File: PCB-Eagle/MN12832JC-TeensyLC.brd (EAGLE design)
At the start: 206.7 x 45.7 mm, 46 parts, among them IC4 ZXBM5210, IC6 74HC132D, SW3 EC12E_SW, SW4 EC12E_SW

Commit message: fixed Up Converter R9/R10 twist, adjusted values for 50V
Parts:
- R10: value 1k -> 39
- R9: value 39 -> 1.5k
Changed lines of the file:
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@@
 <?xml version="1.0" encoding="utf-8"?>
 <!DOCTYPE eagle SYSTEM "eagle.dtd">
-<eagle version="9.5.2">
+<eagle version="9.5.1">
 <drawing>
 <settings>
@@
 <layers>
 <layer number="1" name="Top" color="4" fill="1" visible="yes" active="yes"/>
-<layer number="16" name="Bottom" color="1" fill="1" visible="yes" active="yes"/>
+<layer number="16" name="Bottom" color="1" fill="1" visible="no" active="yes"/>
 <layer number="17" name="Pads" color="2" fill="1" visible="yes" active="yes"/>
 <layer number="18" name="Vias" color="2" fill="1" visible="yes" active="yes"/>
@@
 <layer number="20" name="Dimension" color="24" fill="1" visible="yes" active="yes"/>
 <layer number="21" name="tPlace" color="7" fill="1" visible="yes" active="yes"/>
-<layer number="22" name="bPlace" color="7" fill="1" visible="yes" active="yes"/>
+<layer number="22" name="bPlace" color="7" fill="1" visible="no" active="yes"/>
 <layer number="23" name="tOrigins" color="15" fill="1" visible="yes" active="yes"/>
 <layer number="24" name="bOrigins" color="15" fill="1" visible="yes" active="yes"/>
@@
 <attribute name="NAME" x="123.19" y="19.05" size="1.27" layer="25" rot="R270"/>
 <attribute name="SPICEPREFIX" value="C" x="121.92" y="17.78" size="1.778" layer="27" rot="R270" display="off"/>
-<attribute name="VALUE" x="119.38" y="19.05" size="1.27" layer="27" rot="R270"/>
+<attribute name="VALUE" x="120.142" y="13.716" size="1.27" layer="27"/>
 </element>
 <element name="R8" library="rcl" library_urn="urn:adsk.eagle:library:334" package="R1206" package3d_urn="urn:adsk.eagle:package:23540/2" value="2.7k" x="125.73" y="17.78" smashed="yes" rot="R270">
 <attribute name="NAME" x="127" y="19.05" size="1.27" layer="25" rot="R270"/>
 <attribute name="SPICEPREFIX" value="R" x="125.73" y="17.78" size="1.778" layer="27" rot="R270" display="off"/>
-<attribute name="VALUE" x="123.19" y="19.05" size="1.27" layer="27" rot="R270"/>
+<attribute name="VALUE" x="124.333" y="13.716" size="1.27" layer="27"/>
 </element>
 <element name="IC4" library="vfds" package="SO8" value="ZXBM5210" x="134.62" y="35.56" smashed="yes" rot="R180">
 <attribute name="NAME" x="137.795" y="37.465" size="1.27" layer="25" rot="R270"/>
 <attribute name="PARTNAME" value="ZXBM5210" x="134.62" y="35.56" size="1.778" layer="27" rot="R180" display="off"/>
-<attribute name="VALUE" x="130.175" y="37.465" size="1.27" layer="27" rot="R270"/>
+<attribute name="VALUE" x="130.429" y="38.989" size="1.27" layer="27"/>
 </element>
 <element name="IC5" library="vfds" package="TO263-5" package3d_urn="urn:adsk.eagle:package:16438/2" value="" x="92.71" y="30.48" smashed="yes">
@@
 <attribute name="VALUE" x="106.299" y="33.401" size="1.27" layer="27" rot="R90"/>
 </element>
-<element name="R9" library="rcl" library_urn="urn:adsk.eagle:library:334" package="R1206" package3d_urn="urn:adsk.eagle:package:23540/2" value="39" x="95.25" y="19.05" smashed="yes">
+<element name="R9" library="rcl" library_urn="urn:adsk.eagle:library:334" package="R1206" package3d_urn="urn:adsk.eagle:package:23540/2" value="1.5k" x="95.25" y="19.05" smashed="yes">
 <attribute name="NAME" x="93.98" y="20.32" size="1.27" layer="25"/>
 <attribute name="SPICEPREFIX" value="R" x="95.25" y="19.05" size="1.778" layer="27" display="off"/>
 <attribute name="VALUE" x="93.98" y="16.51" size="1.27" layer="27"/>
 </element>
-<element name="R10" library="rcl" library_urn="urn:adsk.eagle:library:334" package="R1206" package3d_urn="urn:adsk.eagle:package:23540/2" value="1k" x="88.9" y="19.05" smashed="yes">
+<element name="R10" library="rcl" library_urn="urn:adsk.eagle:library:334" package="R1206" package3d_urn="urn:adsk.eagle:package:23540/2" value="39" x="88.9" y="19.05" smashed="yes">
 <attribute name="NAME" x="87.63" y="20.32" size="1.27" layer="25"/>
 <attribute name="SPICEPREFIX" value="R" x="88.9" y="19.05" size="1.778" layer="27" display="off"/>
@@
 <attribute name="NAME" x="132.08" y="26.67" size="1.27" layer="25" rot="R180"/>
 <attribute name="SPICEPREFIX" value="R" x="130.81" y="27.94" size="1.778" layer="27" rot="R180" display="off"/>
-<attribute name="VALUE" x="132.08" y="30.48" size="1.27" layer="27" rot="R180"/>
+<attribute name="VALUE" x="133.35" y="30.48" size="1.27" layer="27" rot="R180"/>
 </element>
 <element name="R12" library="rcl" library_urn="urn:adsk.eagle:library:334" package="0411/15" package3d_urn="urn:adsk.eagle:package:23568/1" value="22" x="140.97" y="31.75" smashed="yes" rot="R270">

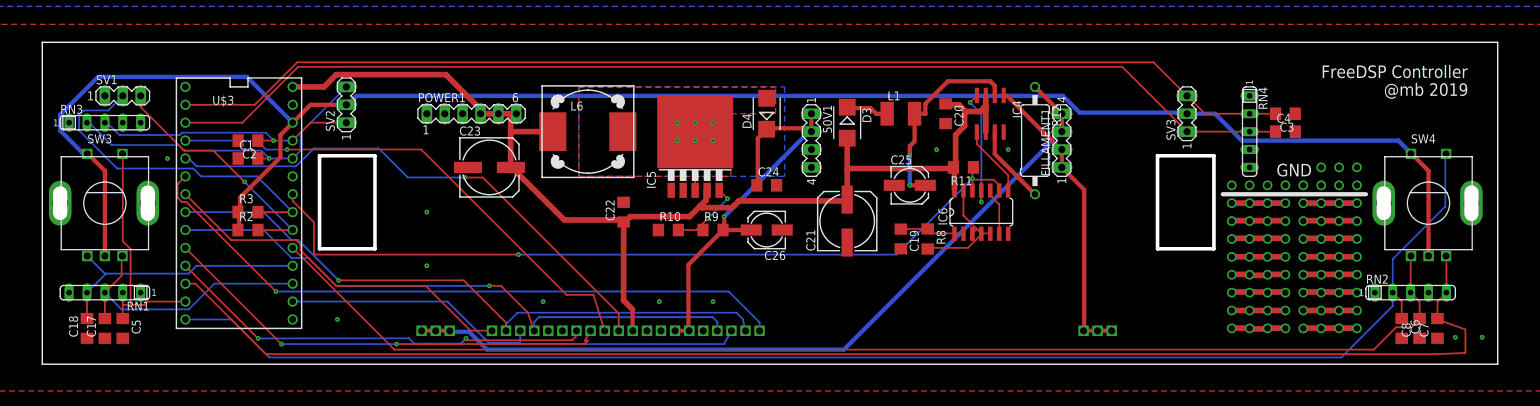
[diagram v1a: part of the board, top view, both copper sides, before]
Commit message: Added Voltage drop diode for Vdd1, lowered Fillament frequency to avoid off time
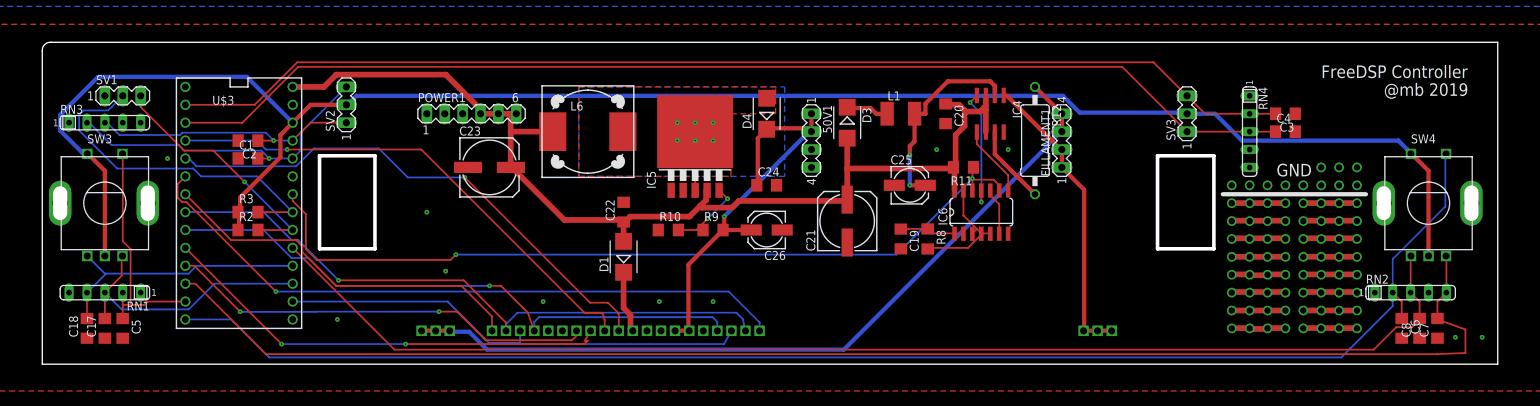
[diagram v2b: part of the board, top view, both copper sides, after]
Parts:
- added D1: (no value), diode:SMB
- C19: value 4.7n -> 100n
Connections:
- new net N$3: D1.C, U$1.VDD1
- net +5V: now also D1.A; no longer U$1.VDD1
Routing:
- net +5V: track 167.3 -> 154.1 mm
- net N$3: track 0.00 -> 8.85 mm
- net BLK2: track 52.0 -> 53.2 mm
- net FF_BLANK: track 116.0 -> 116.9 mm
- net GSIN: track 61.5 -> 60.9 mm
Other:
- outline, holes or cut-outs redrawn

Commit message: minor stuff
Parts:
- R11, R8: value 2.7k -> 4.7k
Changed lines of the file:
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@@
 <attribute name="VALUE" x="120.142" y="13.716" size="1.27" layer="27"/>
 </element>
-<element name="R8" library="rcl" library_urn="urn:adsk.eagle:library:334" package="R1206" package3d_urn="urn:adsk.eagle:package:23540/2" value="2.7k" x="125.73" y="17.78" smashed="yes" rot="R270">
+<element name="R8" library="rcl" library_urn="urn:adsk.eagle:library:334" package="R1206" package3d_urn="urn:adsk.eagle:package:23540/2" value="4.7k" x="125.73" y="17.78" smashed="yes" rot="R270">
 <attribute name="NAME" x="127" y="19.05" size="1.27" layer="25" rot="R270"/>
 <attribute name="SPICEPREFIX" value="R" x="125.73" y="17.78" size="1.778" layer="27" rot="R270" display="off"/>
@@
 <attribute name="VALUE" x="130.175" y="20.828" size="1.27" layer="27" ratio="10"/>
 </element>
-<element name="R11" library="rcl" library_urn="urn:adsk.eagle:library:334" package="R1206" package3d_urn="urn:adsk.eagle:package:23540/2" value="2.7k" x="130.81" y="27.94" smashed="yes" rot="R180">
+<element name="R11" library="rcl" library_urn="urn:adsk.eagle:library:334" package="R1206" package3d_urn="urn:adsk.eagle:package:23540/2" value="4.7k" x="130.81" y="27.94" smashed="yes" rot="R180">
 <attribute name="NAME" x="132.08" y="26.67" size="1.27" layer="25" rot="R180"/>
 <attribute name="SPICEPREFIX" value="R" x="130.81" y="27.94" size="1.778" layer="27" rot="R180" display="off"/>

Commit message: added FreeDSP controller. Reads Levels. Sets Volume.
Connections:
- net N$1 renamed SCL
- net N$2 renamed SDA
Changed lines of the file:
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@@
 <wire x1="147.955" y1="5.08" x2="147.861" y2="4.731" width="0.6096" layer="1"/>
 </signal>
-<signal name="N$1">
+<signal name="SCL">
 <contactref element="SV1" pad="2"/>
 <contactref element="U$3" pad="19/A5"/>
@@
 <wire x1="35.56" y1="21.59" x2="30.48" y2="26.67" width="0.25" layer="16"/>
 </signal>
-<signal name="N$2">
+<signal name="SDA">
 <contactref element="SV1" pad="3"/>
 <contactref element="U$3" pad="18/A4"/>
